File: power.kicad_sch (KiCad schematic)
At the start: 49 parts, among them J1 Battery 1, J7 Battery 2, J8 USB, U1 AMS1117-3.3, U5 TPS56A37RPAR, U6 TPS56A37RPAR

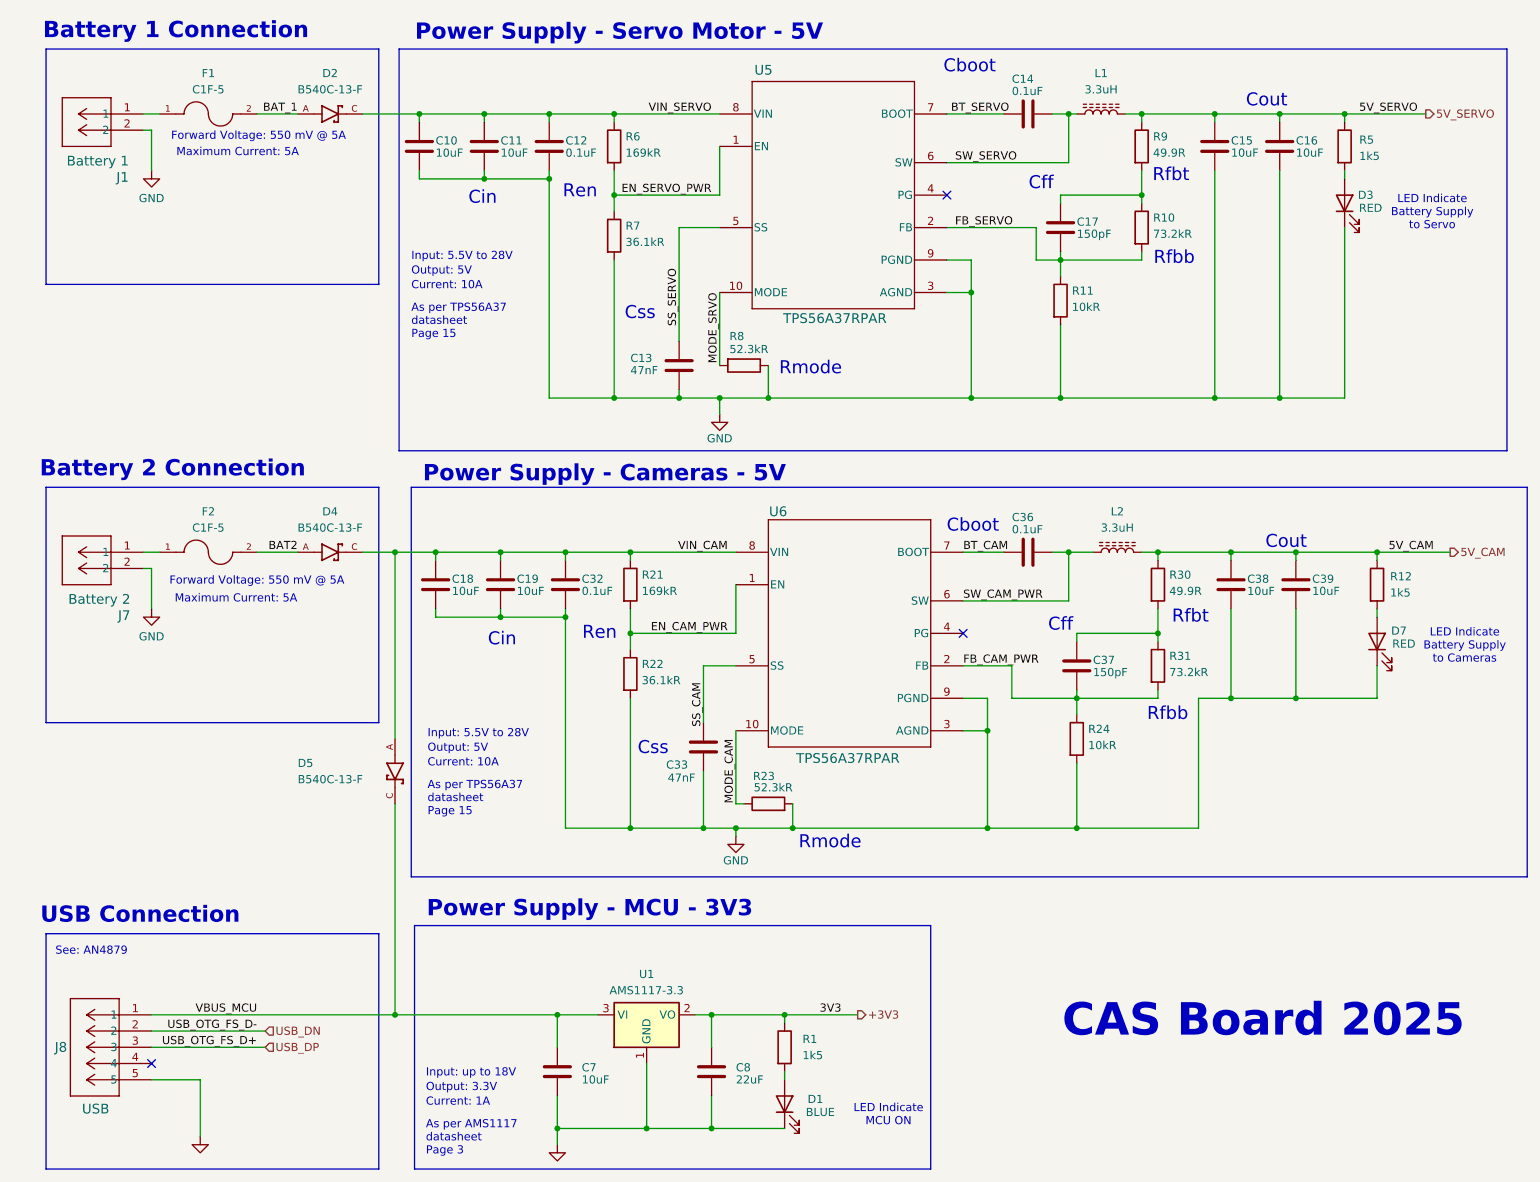
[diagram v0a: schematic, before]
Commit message: remove camera power and interface headers and pins from schematic and PCB
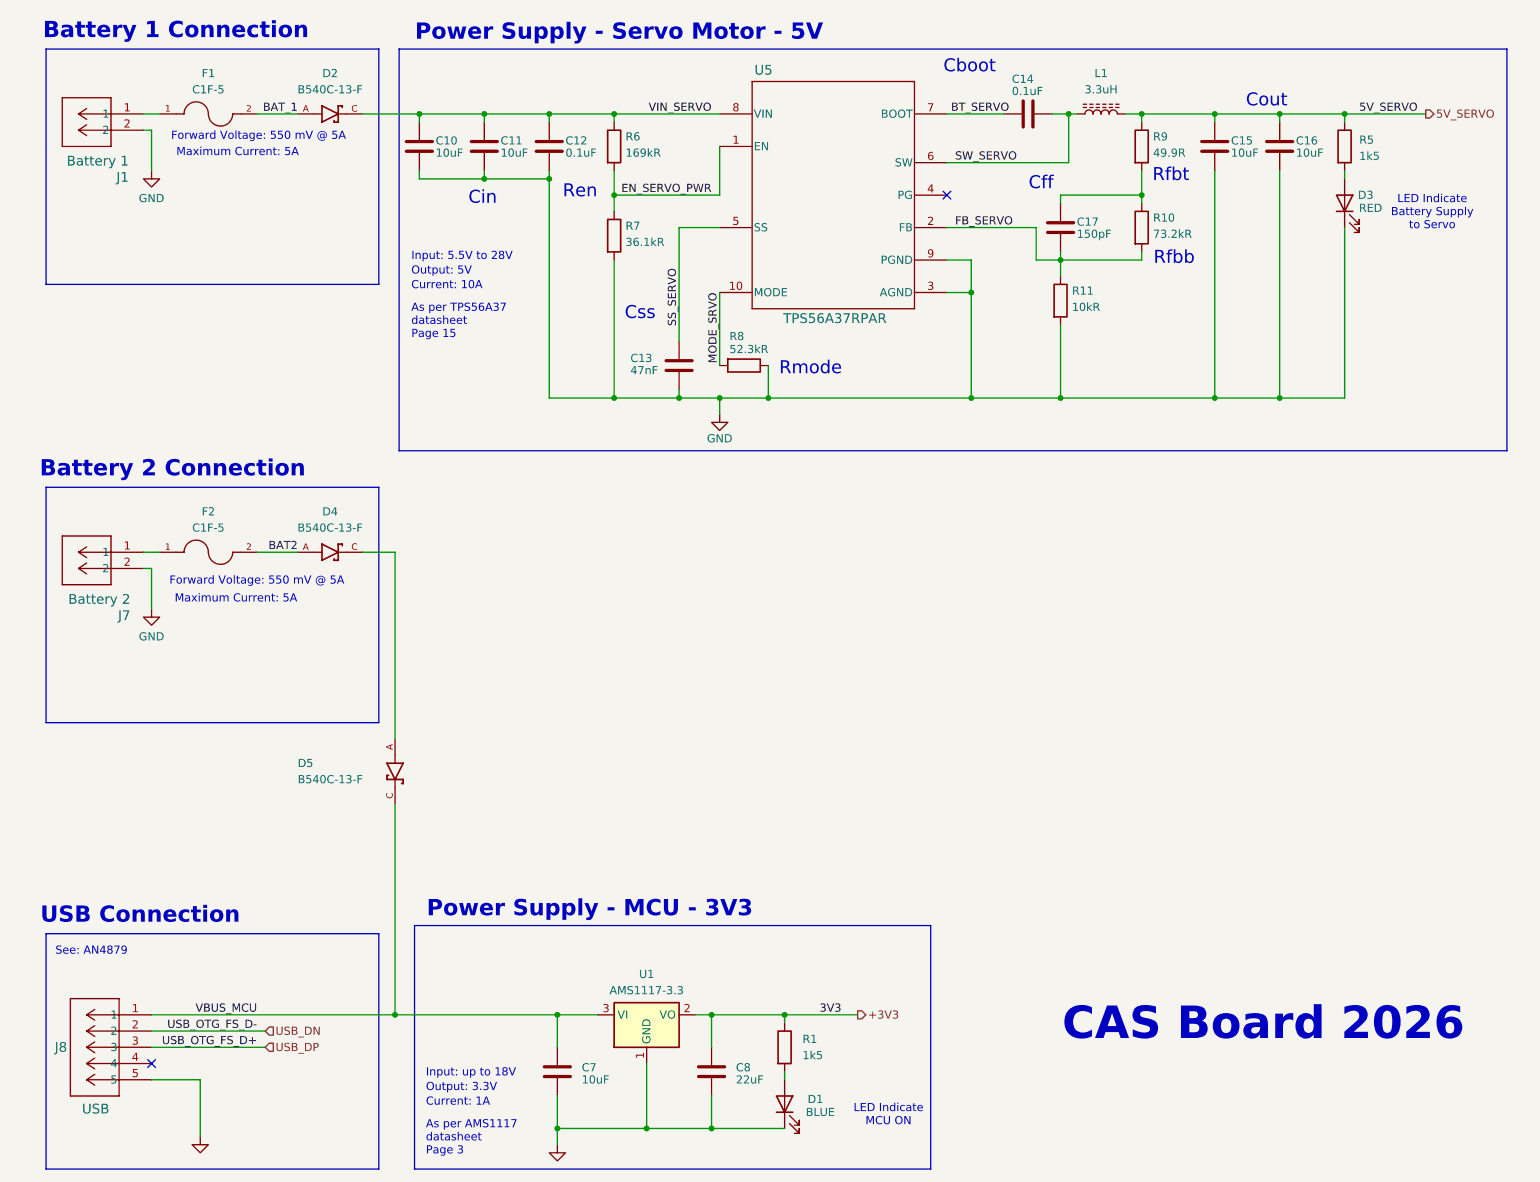
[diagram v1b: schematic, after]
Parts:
- removed C18, C19, C38, C39: 10uF, Capacitor_SMD:C_0805_2012Metric, symbol Device:C
- removed C32, C36: 0.1uF, Capacitor_SMD:C_0805_2012Metric, symbol Device:C
- removed C33: 47nF, Capacitor_SMD:C_0805_2012Metric, symbol Device:C
- removed C37: 150pF, Capacitor_SMD:C_0805_2012Metric, symbol Device:C
- removed D7: RED, LED_SMD:LED_0805_2012Metric, symbol Device:LED
- removed L2: 3.3uH, Inductor_SMD:L_0805_2012Metric_Pad1.05x1.20mm_HandSolder, symbol Device:L_Ferrite
- removed R12: 1k5, Resistor_SMD:R_0805_2012Metric_Pad1.20x1.40mm_HandSolder, symbol Device:R
- removed R21: 169kR, Capacitor_SMD:C_0805_2012Metric, symbol Device:R
- removed R22: 36.1kR, Capacitor_SMD:C_0805_2012Metric, symbol Device:R
- removed R23: 52.3kR, Capacitor_SMD:C_0805_2012Metric, symbol Device:R
- removed R24: 10kR, Capacitor_SMD:C_0805_2012Metric, symbol Device:R
- removed R30: 49.9R, Capacitor_SMD:C_0805_2012Metric, symbol Device:R
- removed R31: 73.2kR, Capacitor_SMD:C_0805_2012Metric, symbol Device:R
- removed U6: TPS56A37RPAR, RPA0010A-MFG, symbol TPS56A37RPAR:TPS56A37RPAR
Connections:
- net VIN_CAM: no longer names the net of D4.C, D5.A
- no-connect marks 3 -> 2
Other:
- note added: "CAS Board 2026"
- note removed: "CAS Board 2025"
- note removed: "LED Indicate Battery Supply to Cameras"
- note removed: "Power Supply - Cameras - 5V"
